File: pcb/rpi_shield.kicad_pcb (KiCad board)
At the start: 2 copper layers, 65 x 56 mm, 26 parts, among them P101 CONN_01X02, P102 CONN_02X20, P201 CONN_01X01, P202 CONN_01X01, P203 CONN_01X01, P204 CONN_01X01, Q201 AM4874N, Q202 AM4874N, Q203 AM4874N, Q204 AM4874N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

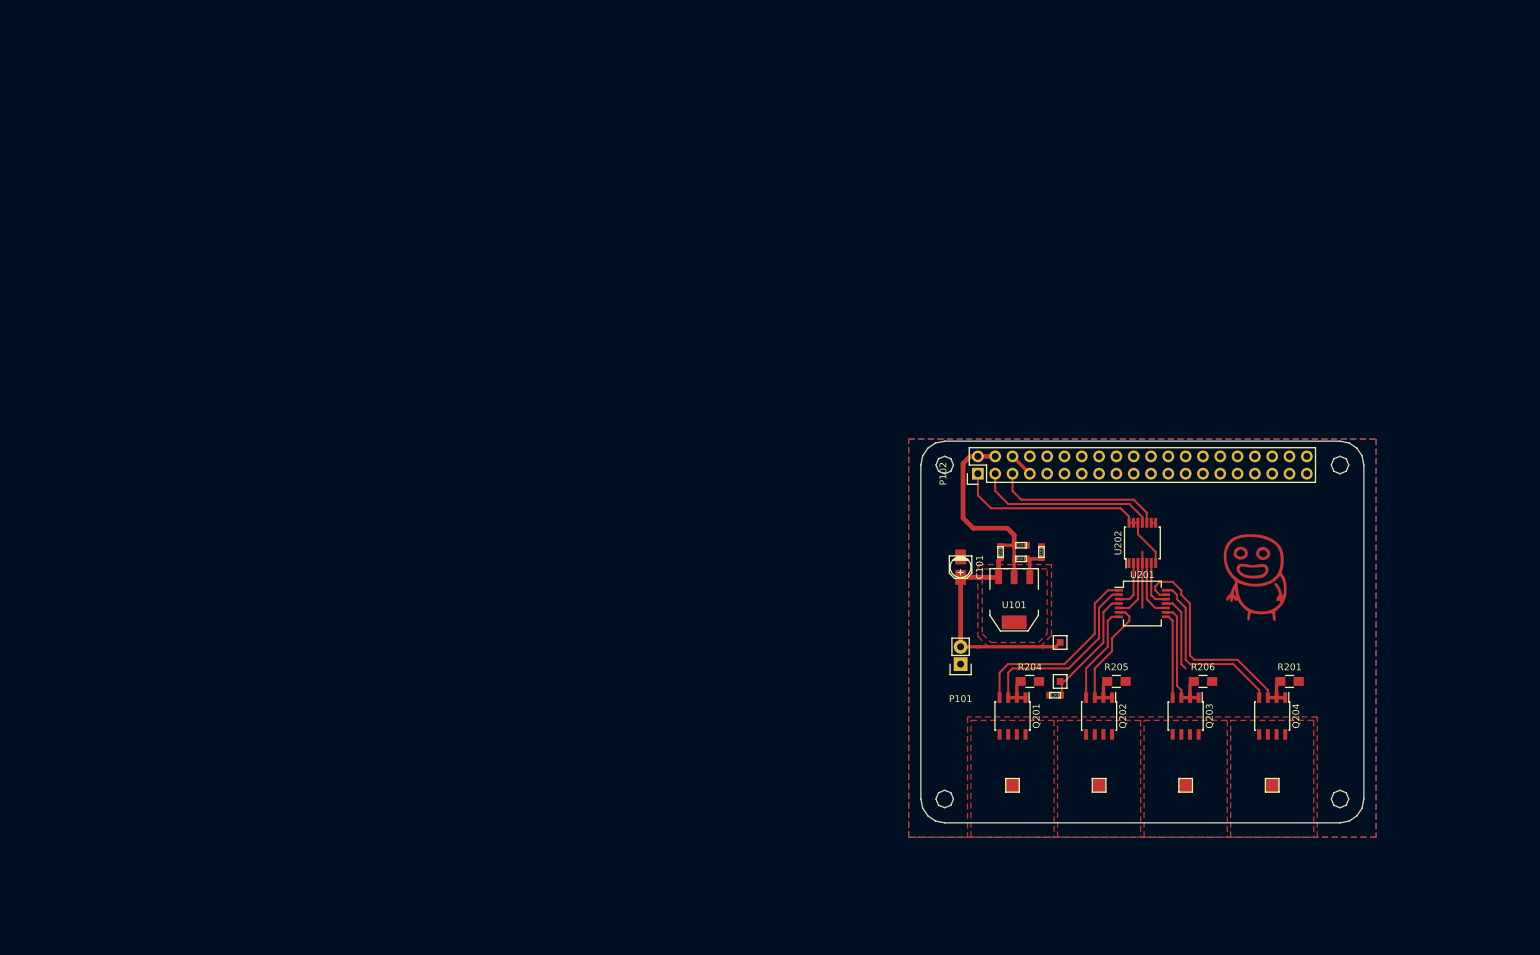
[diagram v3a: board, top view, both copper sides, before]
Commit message: changed fets, added usb serial
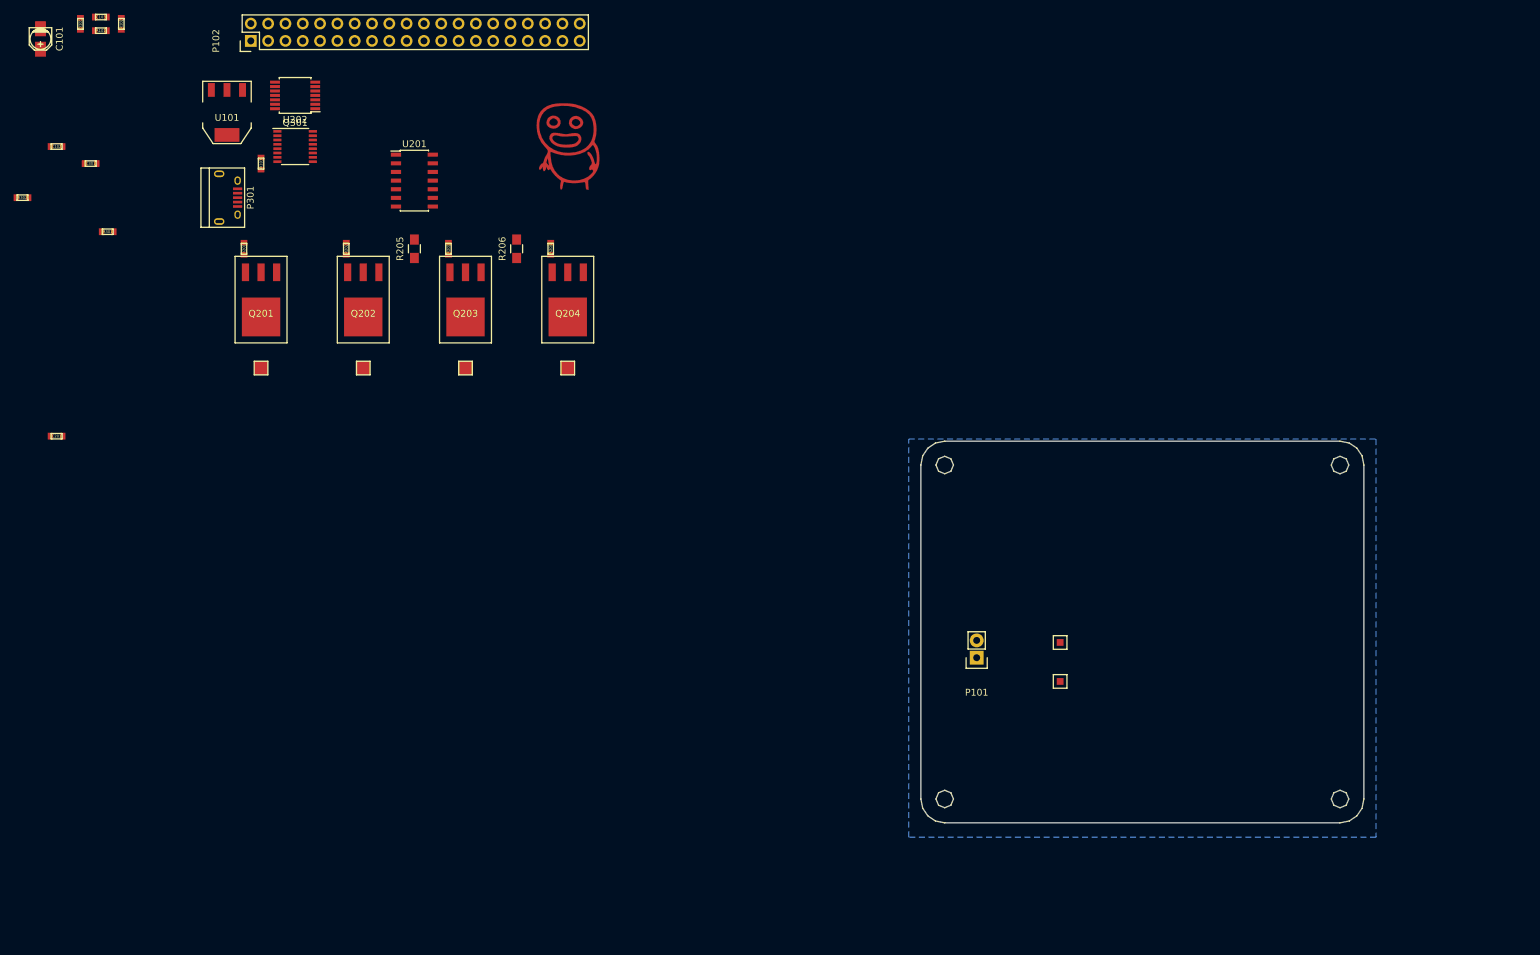
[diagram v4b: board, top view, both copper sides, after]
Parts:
- added C102: C, netl:SMD_0603, F.Cu at (-28.5, 15.5)
- added C301: 100n, netl:SMD_0603, F.Cu at (-23.5, 18.0)
- added P301: USB_OTG, Connect:USB_Micro-B, F.Cu at (-3.50, 23.0)
- added Q301: FT230XS-R, Housings_SSOP:SSOP-16_3.9x4.9mm_Pitch0.635mm, F.Cu at (6.50, 15.5)
- added R103: 0R, netl:SMD_0603, F.Cu at (1.50, 18.0)
- added R202: R, netl:SMD_0603, F.Cu at (14.0, 30.5)
- added R203: R, netl:SMD_0603, F.Cu at (29.0, 30.5)
- added R301: 10k, netl:SMD_0603, F.Cu at (-21.0, 28.0)
- added R302: 10k, netl:SMD_0603, F.Cu at (-33.5, 23.0)
- Q201, Q202, Q203, Q204: value AM4874N -> Q_NMOS_GDSD; footprint Housings_SOIC:SOIC-8_3.9x4.9mm_Pitch1.27mm -> netl:TO252
- R201, R204: footprint Resistors_SMD:R_0805_HandSoldering -> netl:SMD_0603
- U201: footprint Housings_SSOP:SSOP-14_5.3x6.2mm_Pitch0.65mm -> Housings_SOIC:SOIC-14_3.9x8.7mm_Pitch1.27mm
- moved R201 166.0 mm to (-1.00, 30.5), turned to 90 degrees
- moved C101 155.7 mm to (-30.9, -0.28)
- moved C103 155.7 mm to (-22.0, -3.50)
- moved D101 155.7 mm to (-25.0, -2.50)
- moved R101 155.7 mm to (-22.0, -1.50)
- moved R102 155.7 mm to (-19.0, -2.50)
- moved C201 151.3 mm to (-28.5, 58.0)
- moved U202 140.6 mm to (6.50, 8.00), turned to 180 degrees
- moved U101 135.8 mm to (-3.50, 10.5)
- moved P201 126.1 mm to (1.50, 48.0)
- moved Q201 124.8 mm to (1.50, 40.5), turned to 180 degrees
- moved P102 124.1 mm to (0.00, 0.00)
- moved P202 124.1 mm to (16.5, 48.0)
- moved U201 123.5 mm to (24.0, 20.5)
- moved Q202 122.8 mm to (16.5, 40.5), turned to 180 degrees
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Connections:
- net B renamed /LED driver/B
- net G renamed /LED driver/G
- net R renamed /LED driver/R
- net SCL renamed /LED driver/SCL
- net SDA renamed /LED driver/SDA
- net W renamed /LED driver/W
- P102 pad 10: Net-(P102-Pad10) -> /USBSerial/TX
- P102 pad 8: Net-(P102-Pad8) -> /USBSerial/RX
- Q201 pad 2: Net-(Q201-Pad1) -> /LED driver/DrainRed
- Q201 pad 3: Net-(Q201-Pad1) -> Net-(Q201-Pad3)
- Q201 pad 4: Net-(Q201-Pad4) -> /LED driver/DrainRed
- Q202 pad 2: Net-(Q202-Pad1) -> /LED driver/DrainGreen
- Q202 pad 3: Net-(Q202-Pad1) -> Net-(Q202-Pad3)
- Q202 pad 4: Net-(Q202-Pad4) -> /LED driver/DrainGreen
- Q203 pad 2: Net-(Q203-Pad1) -> /LED driver/DrainBlue
- Q203 pad 3: Net-(Q203-Pad1) -> Net-(Q203-Pad3)
- Q203 pad 4: Net-(Q203-Pad4) -> /LED driver/DrainBlue
- Q204 pad 2: Net-(Q204-Pad1) -> /LED driver/DrainWhite
- Q204 pad 3: Net-(Q204-Pad1) -> Net-(Q204-Pad3)
- Q204 pad 4: Net-(Q204-Pad4) -> /LED driver/DrainWhite
- R201 pad 1: Net-(Q204-Pad1) -> Net-(Q201-Pad3)
- R204 pad 1: Net-(Q201-Pad1) -> Net-(Q204-Pad3)
- U201 pad 1: Net-(Q201-Pad4) -> Net-(Q201-Pad1)
- U201 pad 13: Net-(Q204-Pad1) -> Net-(Q204-Pad3)
- U201 pad 14: Net-(Q204-Pad4) -> Net-(Q204-Pad1)
- U201 pad 2: Net-(Q201-Pad1) -> Net-(Q201-Pad3)
- U201 pad 6: Net-(Q202-Pad1) -> Net-(Q202-Pad3)
- U201 pad 7: Net-(Q202-Pad4) -> Net-(Q202-Pad1)
- U201 pad 8: Net-(Q203-Pad4) -> Net-(Q203-Pad1)
- U201 pad 9: Net-(Q203-Pad1) -> Net-(Q203-Pad3)
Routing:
- net Vdd: track 51.5 -> 0.00 mm
- net Net-(Q204-Pad1): track 36.9 -> 0.00 mm
- net 3v3: track 35.8 -> 0.00 mm
- net Net-(Q201-Pad1): track 32.4 -> 0.00 mm
- net 5V: track 30.5 -> 0.00 mm
- net Net-(Q201-Pad4): track 28.8 -> 0.00 mm
- net /LED driver/SDA: track 27.3 -> 0.00 mm
- net Net-(Q204-Pad4): track 25.7 -> 0.00 mm
- net /LED driver/SCL: track 25.0 -> 0.00 mm
- net GND: track 23.8 -> 0.00 mm
- net Net-(Q202-Pad1): track 21.0 -> 0.00 mm
- net Net-(Q203-Pad1): track 18.9 -> 0.00 mm
- net Net-(Q202-Pad4): track 14.5 -> 0.00 mm
- net Net-(Q203-Pad4): track 12.6 -> 0.00 mm
- net /LED driver/G: track 8.65 -> 0.00 mm
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- removed copper zone on F.Cu, net /LED driver/DrainBlue
- removed copper zone on F.Cu, net /LED driver/DrainGreen
- removed copper zone on F.Cu, net /LED driver/DrainRed
- removed copper zone on F.Cu, net /LED driver/DrainWhite
- removed copper zone on F.Cu, net 5V
- removed copper zone on F.Cu, net GND

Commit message: ready for etching!
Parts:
- removed C101: C, Capacitors_SMD:c_elec_3x5.3
- removed C102, C103: C, netl:SMD_0603
- removed D101: D, netl:SMD_0603
- removed JP11 (x2): CONN_01X01, netl:1Pin_small
- removed P101: CONN_01X02, Pin_Headers:Pin_Header_Straight_1x02
- removed R101, R102: R, netl:SMD_0603
- removed R205, R206: R, Resistors_SMD:R_0805_HandSoldering
- removed U101: LM317AEMP, TO_SOT_Packages_SMD:SOT-223
- added C202: 100n, netl:SMD_0603, F.Cu at (133.6, 86.4)
- added C203: 100n, netl:SMD_0603, F.Cu at (146.0, 82.8)
- C201: value C -> 100n
- R201, R202, R203, R204: footprint netl:SMD_0603 -> Resistors_SMD:R_1206
- moved C301 182.1 mm to (141.4, 95.2), turned to 90 degrees
- moved C201 181.9 mm to (147.8, 102.9)
- moved R302 179.6 mm to (132.5, 91.4), turned to 90 degrees
- moved R301 174.8 mm to (137.6, 101.3), turned to 90 degrees
- moved P201 169.1 mm to (150.3, 128.3)
- moved P202 158.2 mm to (152.9, 128.3)
- moved U202 154.3 mm to (140.2, 85.1)
- moved Q204 154.2 mm to (178.3, 120.6)
- moved R204 154.2 mm to (173.0, 115.0), turned to 270 degrees
- moved U201 154.0 mm to (154.1, 102.9)
- moved Q301 153.5 mm to (137.7, 95.2), turned to 270 degrees
- moved R203 153.4 mm to (157.0, 115.0), turned to 270 degrees
- moved Q203 153.3 mm to (162.2, 120.6)
- moved P102 152.6 mm to (130.0, 80.0)
- moved R202 152.5 mm to (141.0, 115.0), turned to 270 degrees
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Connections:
- C201 pad 2: Vdd -> 5V
- P301 pad 6: Net-(P301-Pad6) -> GND
- Q301 pad 10: Net-(C301-Pad2) -> Net-(Q301-Pad10)
- U201 pad 4: Vdd -> 5V
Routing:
- net 5V: track 0.00 -> 45.6 mm, vias 0 -> 2
- net Net-(Q201-Pad3): track 0.00 -> 39.4 mm
- net GND: track 0.00 -> 32.1 mm, vias 0 -> 4
- net Net-(Q204-Pad1): track 0.00 -> 31.1 mm
- net /LED driver/B: track 0.00 -> 29.1 mm
- net Net-(Q204-Pad3): track 0.00 -> 29.1 mm
- net /LED driver/G: track 0.00 -> 27.6 mm
- net /LED driver/W: track 0.00 -> 27.3 mm
- net Net-(Q201-Pad1): track 0.00 -> 27.1 mm
- net /LED driver/R: track 0.00 -> 23.5 mm
- net /LED driver/DrainWhite: track 0.00 -> 23.5 mm
- net /LED driver/DrainRed: track 0.00 -> 23.5 mm
- net 3v3: track 0.00 -> 21.3 mm
- net /USBSerial/5VUSB: track 0.00 -> 17.9 mm
- net /USBSerial/RX: track 0.00 -> 16.4 mm
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- added copper zone on F.Cu, net GND
- removed copper zone on B.Cu, net GND
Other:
- outline, holes or cut-outs redrawn

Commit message: ready for etching!
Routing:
- net GND: track 32.1 -> 30.7 mm
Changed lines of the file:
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@@
     (thickness 1.6)
     (drawings 173)
-    (tracks 186)
+    (tracks 185)
     (zones 0)
     (modules 25)
@@
   (segment (start 143.11 85.08) (end 141.303 85.08) (width 0.3) (layer F.Cu) (net 1))
   (segment (start 137.62 80) (end 135.08 77.46) (width 0.5) (layer F.Cu) (net 1))
-  (segment (start 143.11 85.08) (end 144.478 85.08) (width 0.3) (layer F.Cu) (net 1))
   (segment (start 137.21 83.78) (end 135.872 83.78) (width 0.3) (layer F.Cu) (net 1))
   (segment (start 135.872 83.78) (end 135.842 83.81) (width 0.3) (layer F.Cu) (net 1))

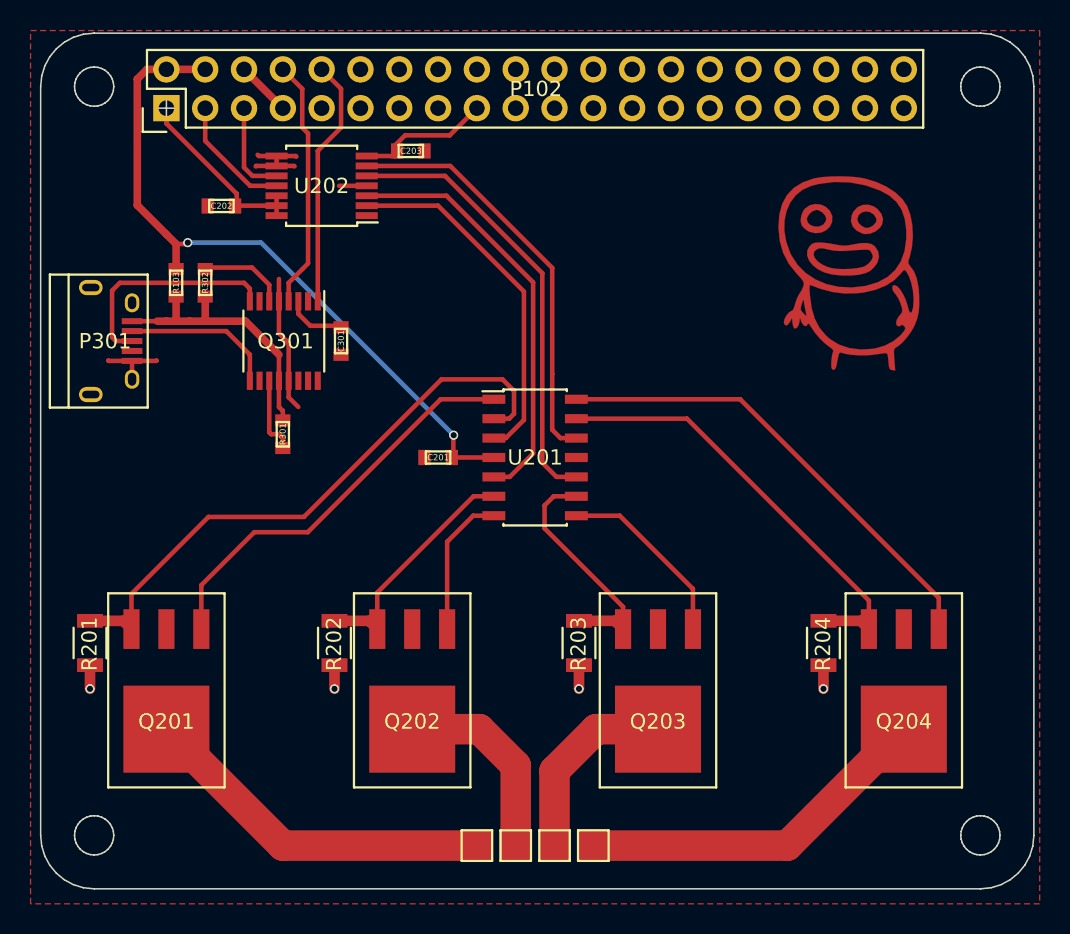
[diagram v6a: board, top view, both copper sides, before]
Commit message: started work on 2 layered version
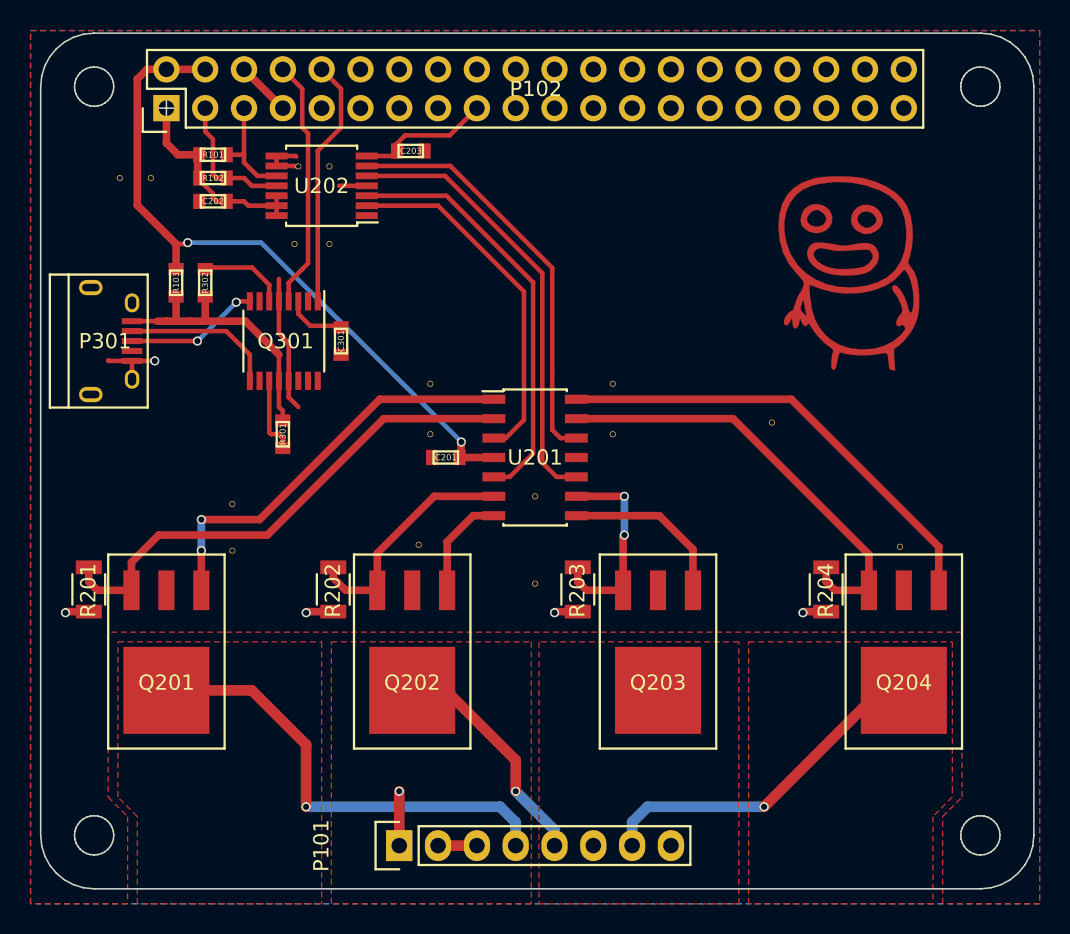
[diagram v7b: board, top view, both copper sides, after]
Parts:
- removed P201, P202, P203, P204: CONN_01X01, netl:1Pin_big
- added P101: CONN_01X08, Pin_Headers:Pin_Header_Straight_1x08, F.Cu at (145.2, 128.3)
- added R101: 10k, netl:SMD_0603, F.Cu at (133.0, 83.0)
- added R102: 10k, netl:SMD_0603, F.Cu at (133.0, 84.6)
- added VIA: via, netl:via, F.Cu at (127.0, 84.6)
- added VIA: via, netl:via, F.Cu at (134.3, 105.9)
- added VIA: via, netl:via, F.Cu at (134.3, 109.0)
- added VIA: via, netl:via, F.Cu at (147.3, 98.0)
- added VIA: via, netl:via, F.Cu at (147.3, 101.3)
- added VIA: via, netl:via, F.Cu at (140.7, 83.8)
- added VIA: via, netl:via, F.Cu at (138.6, 83.8)
- added VIA: via, netl:via, F.Cu at (140.7, 88.9)
- added VIA: via, netl:via, F.Cu at (138.4, 88.9)
- added VIA: via, netl:via, F.Cu at (129.0, 84.6)
- added VIA: via, netl:via, F.Cu at (146.5, 108.6)
- added VIA: via, netl:via, F.Cu at (154.1, 111.1)
- added VIA: via, netl:via, F.Cu at (154.1, 105.4)
- added VIA: via, netl:via, F.Cu at (178.0, 108.7)
- added VIA: via, netl:via, F.Cu at (169.6, 100.6)
- added VIA: via, netl:via, F.Cu at (159.2, 98.0)
- added VIA: via, netl:via, F.Cu at (159.2, 101.3)
- moved R204 3.51 mm to (173.2, 111.5)
- moved R201 3.50 mm to (124.9, 111.5)
- moved R202 3.50 mm to (140.9, 111.5)
- moved R203 3.50 mm to (156.9, 111.5)
- moved Q204 2.54 mm to (178.3, 118.1)
- moved Q203 2.54 mm to (162.2, 118.1)
- moved Q202 2.54 mm to (146.1, 118.1)
- moved Q201 2.54 mm to (130.0, 118.1)
- moved C202 0.63 mm to (133.0, 86.1)
- moved C201 0.51 mm to (148.3, 102.9)
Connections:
- net /LED driver/DrainWhite renamed /LED driver/DrainFan
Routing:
- net /LED driver/DrainBlue: track 12.8 -> 0.00 mm
- net /LED driver/DrainRed: track 23.5 -> 30.3 mm, vias 0 -> 1
- net Net-(P301-Pad3): track 14.7 -> 8.79 mm, vias 0 -> 2
- net Net-(Q201-Pad3): track 39.4 -> 33.6 mm
- net VCC: track 0.00 -> 2.54 mm
- net Net-(Q202-Pad1): track 9.48 -> 6.94 mm
- net /LED driver/DrainGreen: track 13.0 -> 15.3 mm, vias 0 -> 1
- net /LED driver/SDA: track 8.03 -> 9.77 mm
- net 3v3: track 21.3 -> 22.6 mm
- net GND: track 30.7 -> 31.9 mm, vias 4 -> 6
- net Net-(Q203-Pad3): track 15.7 -> 14.6 mm, vias 0 -> 2
- net Net-(Q203-Pad1): track 12.2 -> 11.3 mm
- net /LED driver/SCL: track 6.24 -> 7.08 mm
- net Net-(Q204-Pad3): track 29.1 -> 29.8 mm
- net /LED driver/DrainFan: track 23.5 -> 22.9 mm, vias 0 -> 1
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- added copper zone on F.Cu, net /LED driver/DrainBlue
- added copper zone on F.Cu, net /LED driver/DrainFan
- added copper zone on F.Cu, net /LED driver/DrainGreen
- added copper zone on F.Cu, net /LED driver/DrainRed
- added copper zone on B.Cu, net GND
